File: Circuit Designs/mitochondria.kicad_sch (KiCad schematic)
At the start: 97 parts

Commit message: deleted previous version files
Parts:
- C100, C101, C102, C103, C104, C105, C106, C107, C108, C109, C110, C111, C112, C113, C56, C57, C58, C59, C60, C61, C62, C63, C64, C65, C66, C67, C68, C69, C70, C71, C72, C73, C74, C75, C76, C77, C78, C79, C89, C90, C91, C92, C93, C94, C95, C96, C97, C98, C99: renamed from C?; footprint Capacitor_SMD:C_0402_1005Metric -> CoF_Capacitor:C-0402
- C80, C81, C82, C83, C84, C85, C86, C87, C88: renamed from C?; footprint Capacitor_SMD:C_0805_2012Metric -> CoF_Capacitor:C-0805
- R36, R37, R38, R39, R40, R41, R42, R43, R44, R45, R46, R47, R48, R49, R50, R51, R52, R53, R54, R55, R56, R57, R58, R59, R60, R61, R62, R63, R64, R65, R66, R67: renamed from R?; footprint Resistor_SMD:R_0402_1005Metric -> CoF_Resistor:R-0402
- gave numbers to parts that had none: 7

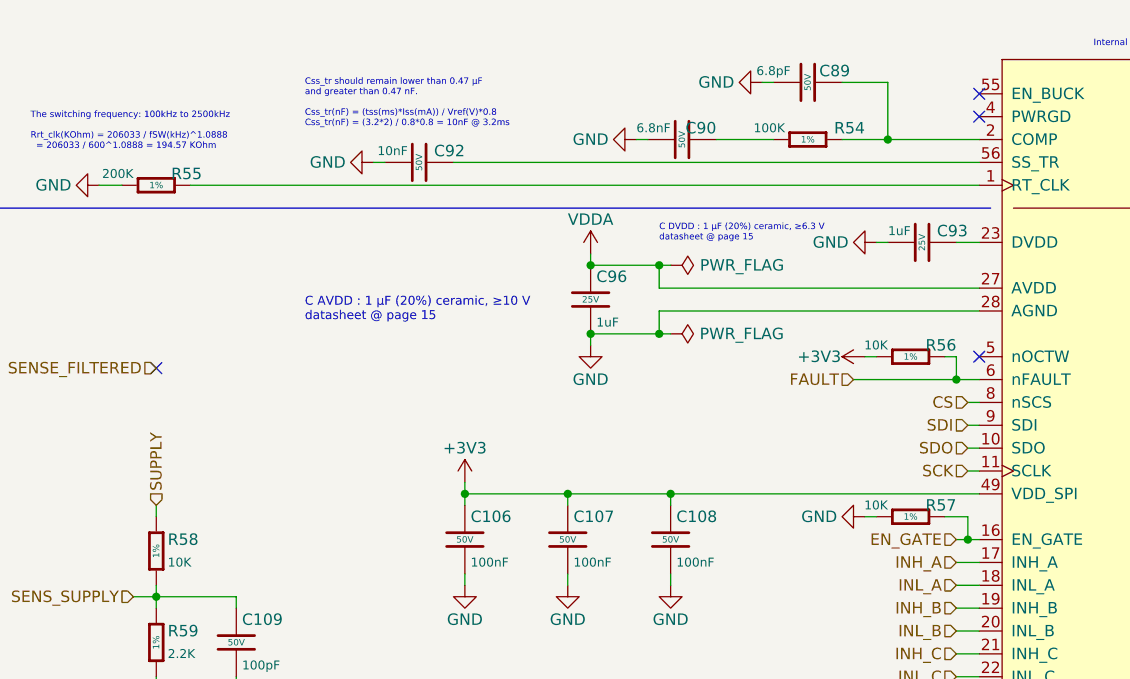
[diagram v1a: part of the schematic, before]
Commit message: changed the LED packages, edited field reference positions
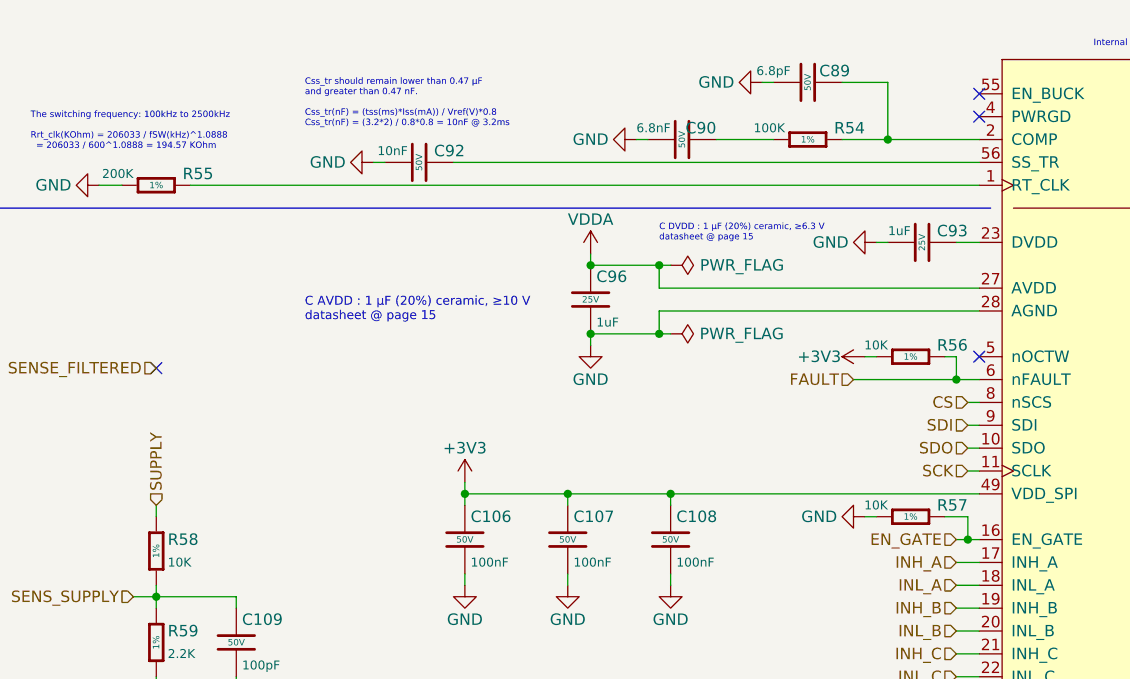
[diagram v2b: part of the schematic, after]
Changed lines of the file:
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@@
   (symbol (lib_id "CoE_Resistor:200K") (at 33.02 99.06 90) (unit 1)
     (in_bom yes) (on_board yes)
-    (property "Reference" "R55" (id 0) (at 38.1 97.79 90)
+    (property "Reference" "R55" (id 0) (at 39.37 97.79 90)
       (effects (font (size 1.27 1.27)) (justify left))
     )
@@
   (symbol (lib_id "CoE_Resistor:10K") (at 116.84 135.89 90) (unit 1)
     (in_bom yes) (on_board yes)
-    (property "Reference" "R57" (id 0) (at 121.92 134.62 90)
+    (property "Reference" "R57" (id 0) (at 123.19 134.62 90)
       (effects (font (size 1.27 1.27)) (justify left))
     )
@@
   (symbol (lib_id "CoE_Resistor:10K") (at 116.84 118.11 90) (unit 1)
     (in_bom yes) (on_board yes)
-    (property "Reference" "R56" (id 0) (at 121.92 116.84 90)
-      (effects (font (size 1.27 1.27)) (justify left))
-    )
+    (property "Reference" "R56" (id 0) (at 123.19 116.84 90)
+      (effects (font (size 1.27 1.27)) (justify left))
+    )

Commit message: added a diode package to the libs
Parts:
- D18: footprint Diode_SMD:D_SOD-123 -> CoF_Diode:SOD-123
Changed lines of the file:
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@@
       (effects (font (size 0.9906 0.9906)) (justify left))
     )
-    (property "Footprint" "Diode_SMD:D_SOD-123" (id 2) (at 224.79 96.52 0)
+    (property "Footprint" "CoF_Diode:SOD-123" (id 2) (at 224.79 96.52 0)
       (effects (font (size 1.27 1.27)) (justify bottom) hide)
     )
-    (property "Datasheet" "https://datasheet.lcsc.com/lcsc/1809140216_Changjiang-Electronics-Tech--CJ-B5819W-SL_C8598.pdf" (id 3) (at 213.106 109.982 0)
+    (property "Datasheet" "https://datasheet.lcsc.com/lcsc/1809140216_Changjiang-Electronics-Tech--CJ-B5819W-SL_C8598.pdf" (id 3) (at 198.12 96.52 0)
       (effects (font (size 1.27 1.27)) hide)
     )

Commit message: created and added the packages called SOT-23-5 and SOT-23-8 to the libraries
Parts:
- U3, U4, U5, U6: footprint Package_TO_SOT_SMD:SOT-23-5 -> CoF_SmallOutline:SOT-23-5
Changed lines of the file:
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@@
       (effects (font (size 0.9906 0.9906)) (justify left))
     )
-    (property "Footprint" "Package_TO_SOT_SMD:SOT-23-5" (id 2) (at 31.115 17.145 0)
-      (effects (font (size 1.27 1.27)) hide)
-    )
-    (property "Datasheet" "https://www.diodes.com/assets/Datasheets/AP2127.pdf" (id 3) (at 31.75 22.86 0)
+    (property "Footprint" "CoF_SmallOutline:SOT-23-5" (id 2) (at 31.115 17.145 0)
+      (effects (font (size 1.27 1.27)) hide)
+    )
+    (property "Datasheet" "https://www.diodes.com/assets/Datasheets/AP2127.pdf" (id 3) (at 31.75 49.53 0)
       (effects (font (size 1.27 1.27)) hide)
     )
@@
       (effects (font (size 0.9906 0.9906)) (justify left))
     )
-    (property "Footprint" "Package_TO_SOT_SMD:SOT-23-5" (id 2) (at 98.425 17.145 0)
-      (effects (font (size 1.27 1.27)) hide)
-    )
-    (property "Datasheet" "https://www.diodes.com/assets/Datasheets/AP2127.pdf" (id 3) (at 99.06 22.86 0)
+    (property "Footprint" "CoF_SmallOutline:SOT-23-5" (id 2) (at 98.425 17.145 0)
+      (effects (font (size 1.27 1.27)) hide)
+    )
+    (property "Datasheet" "https://www.diodes.com/assets/Datasheets/AP2127.pdf" (id 3) (at 99.06 49.53 0)
       (effects (font (size 1.27 1.27)) hide)
     )
@@
       (effects (font (size 0.9906 0.9906)) (justify left))
     )
-    (property "Footprint" "Package_TO_SOT_SMD:SOT-23-5" (id 2) (at 165.735 17.145 0)
-      (effects (font (size 1.27 1.27)) hide)
-    )
-    (property "Datasheet" "https://www.diodes.com/assets/Datasheets/AP2127.pdf" (id 3) (at 166.37 22.86 0)
+    (property "Footprint" "CoF_SmallOutline:SOT-23-5" (id 2) (at 165.735 17.145 0)
+      (effects (font (size 1.27 1.27)) hide)
+    )
+    (property "Datasheet" "https://www.diodes.com/assets/Datasheets/AP2127.pdf" (id 3) (at 166.37 49.53 0)
       (effects (font (size 1.27 1.27)) hide)
     )
@@
       (effects (font (size 0.9906 0.9906)) (justify left))
     )
-    (property "Footprint" "Package_TO_SOT_SMD:SOT-23-5" (id 2) (at 233.045 17.145 0)
-      (effects (font (size 1.27 1.27)) hide)
-    )
-    (property "Datasheet" "https://www.diodes.com/assets/Datasheets/AP2127.pdf" (id 3) (at 233.68 22.86 0)
-      (effects (font (size 1.27 1.27)) hide)
-    )
+    (property "Footprint" "CoF_SmallOutline:SOT-23-5" (id 2) (at 233.045 17.145 0)
+      (effects (font (size 1.27 1.27)) hide)
+    )
+    (property "Datasheet" "https://www.diodes.com/assets/Datasheets/AP2127.pdf" (id 3) (at 233.68 49.53 0)
+      (effects (font (size 1.27 1.27)) hide)
+    )

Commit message: done all the packages and migrations. Now, time to start to route the module
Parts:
- L1: footprint Inductor_SMD:L_Taiyo-Yuden_NR-60xx -> CoF_Inductor:L-7.1-6.6
- U7: footprint Package_SO:HTSSOP-56-1EP_6.1x14mm_P0.5mm_EP3.61x6.35mm -> CoF_SmallOutline:HTSSOP-56-EP

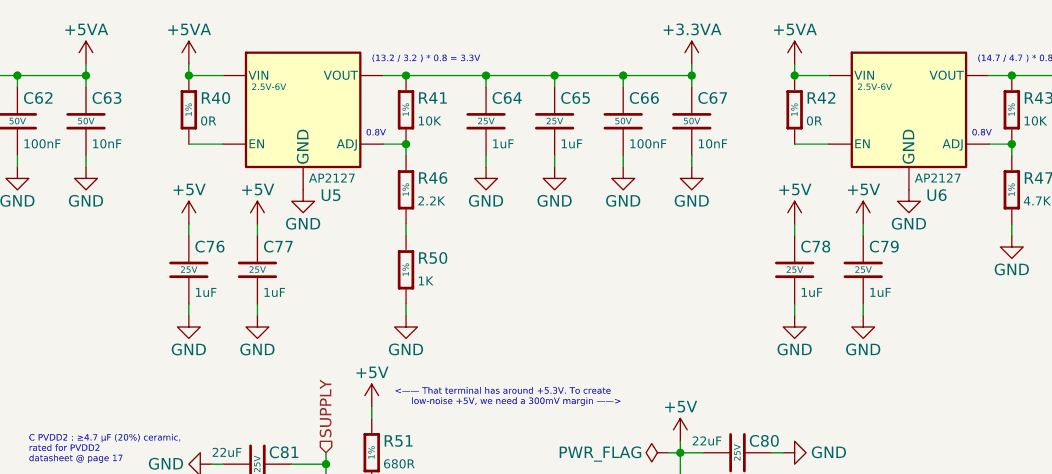
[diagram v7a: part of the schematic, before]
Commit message: First placement of the MCU Page's components are done
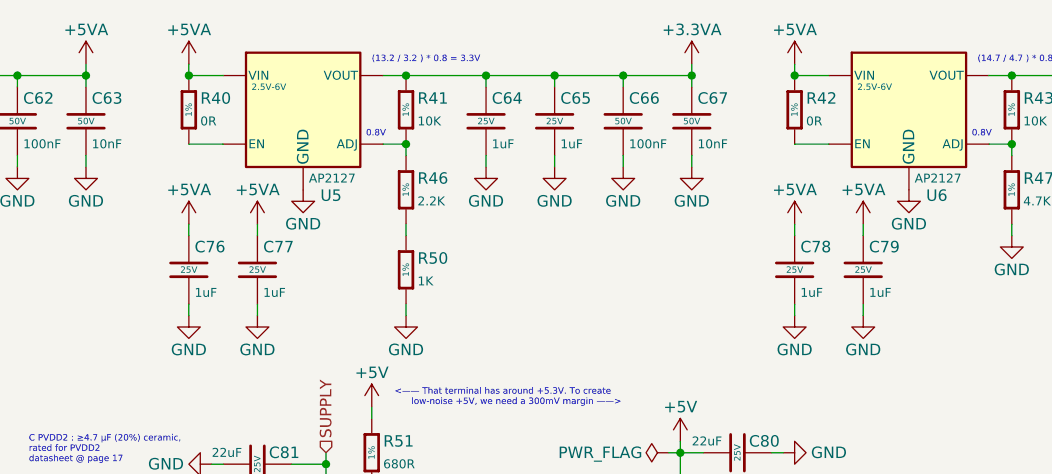
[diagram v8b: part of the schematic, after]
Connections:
- net +5V: no longer C76.1, C77.1, C78.1, C79.1
- net +5VA: now also C76.1, C77.1, C78.1, C79.1
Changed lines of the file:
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@@
-    (pin "1")
-  )
-  (symbol (lib_id "power:+5V") (at 153.67 38.1 0) (unit 1)
-    (in_bom yes) (on_board yes)
-    (property "Reference" "#PWR0112" (id 0) (at 153.67 41.91 0)
-      (effects (font (size 1.27 1.27)) hide)
-    )
-    (property "Value" "+5V" (id 1) (at 153.67 34.29 0))
-    (property "Footprint" "" (id 2) (at 153.67 38.1 0)
-      (effects (font (size 1.27 1.27)) hide)
-    )
-    (property "Datasheet" "" (id 3) (at 153.67 38.1 0)
-      (effects (font (size 1.27 1.27)) hide)
-    )
     (pin "1")
   )
@@
     (pin "2")
   )
-  (symbol (lib_id "power:+5V") (at 161.29 38.1 0) (unit 1)
-    (in_bom yes) (on_board yes)
-    (property "Reference" "#PWR0113" (id 0) (at 161.29 41.91 0)
-      (effects (font (size 1.27 1.27)) hide)
-    )
-    (property "Value" "+5V" (id 1) (at 161.29 34.29 0))
-    (property "Footprint" "" (id 2) (at 161.29 38.1 0)
-      (effects (font (size 1.27 1.27)) hide)
-    )
-    (property "Datasheet" "" (id 3) (at 161.29 38.1 0)
-      (effects (font (size 1.27 1.27)) hide)
-    )
-    (pin "1")
-  )
   (symbol (lib_id "power:GND") (at 93.98 48.26 0) (mirror y) (unit 1)
     (in_bom yes) (on_board yes)
@@
     (pin "1")
   )
-  (symbol (lib_id "power:+5V") (at 220.98 38.1 0) (unit 1)
-    (in_bom yes) (on_board yes)
-    (property "Reference" "#PWR0114" (id 0) (at 220.98 41.91 0)
-      (effects (font (size 1.27 1.27)) hide)
-    )
-    (property "Value" "+5V" (id 1) (at 220.98 34.29 0))
-    (property "Footprint" "" (id 2) (at 220.98 38.1 0)
-      (effects (font (size 1.27 1.27)) hide)
-    )
-    (property "Datasheet" "" (id 3) (at 220.98 38.1 0)
-      (effects (font (size 1.27 1.27)) hide)
-    )
-    (pin "1")
-  )
   (symbol (lib_id "CoE_Capacitor:1uF") (at 228.6 43.18 0) (unit 1)
     (in_bom yes) (on_board yes)
@@
     (pin "1")
     (pin "2")
-  )
-  (symbol (lib_id "power:+5V") (at 228.6 38.1 0) (unit 1)
-    (in_bom yes) (on_board yes)
-    (property "Reference" "#PWR0115" (id 0) (at 228.6 41.91 0)
-      (effects (font (size 1.27 1.27)) hide)
-    )
-    (property "Value" "+5V" (id 1) (at 228.6 34.29 0))
-    (property "Footprint" "" (id 2) (at 228.6 38.1 0)
-      (effects (font (size 1.27 1.27)) hide)
-    )
-    (property "Datasheet" "" (id 3) (at 228.6 38.1 0)
-      (effects (font (size 1.27 1.27)) hide)
-    )
-    (pin "1")
   )
   (symbol (lib_id "power:PWR_FLAG") (at 90.17 115.57 270) (unit 1)
@@
       (effects (font (size 1.27 1.27)) hide)
     )
+    (pin "1")
+  )
+  (symbol (lib_id "power:+5VA") (at 161.29 38.1 0) (unit 1)
+    (in_bom yes) (on_board yes)
+    (property "Reference" "#PWR?" (id 0) (at 161.29 41.91 0)
+      (effects (font (size 1.27 1.27)) hide)
+    )
+    (property "Value" "+5VA" (id 1) (at 161.29 34.29 0))
+    (property "Footprint" "" (id 2) (at 161.29 38.1 0)
+      (effects (font (size 1.27 1.27)) hide)
+    )
+    (property "Datasheet" "" (id 3) (at 161.29 38.1 0)
+      (effects (font (size 1.27 1.27)) hide)
+    )
+    (pin "1")
+  )
+  (symbol (lib_id "power:+5VA") (at 153.67 38.1 0) (unit 1)
+    (in_bom yes) (on_board yes)
+    (property "Reference" "#PWR?" (id 0) (at 153.67 41.91 0)
+      (effects (font (size 1.27 1.27)) hide)
+    )
+    (property "Value" "+5VA" (id 1) (at 153.67 34.29 0))
+    (property "Footprint" "" (id 2) (at 153.67 38.1 0)
+      (effects (font (size 1.27 1.27)) hide)
+    )
+    (property "Datasheet" "" (id 3) (at 153.67 38.1 0)
+      (effects (font (size 1.27 1.27)) hide)
+    )
+    (pin "1")
+  )
+  (symbol (lib_id "power:+5VA") (at 228.6 38.1 0) (unit 1)
+    (in_bom yes) (on_board yes)
+    (property "Reference" "#PWR?" (id 0) (at 228.6 41.91 0)
+      (effects (font (size 1.27 1.27)) hide)
+    )
+    (property "Value" "+5VA" (id 1) (at 228.6 34.29 0))
+    (property "Footprint" "" (id 2) (at 228.6 38.1 0)
+      (effects (font (size 1.27 1.27)) hide)
+    )
+    (property "Datasheet" "" (id 3) (at 228.6 38.1 0)
+      (effects (font (size 1.27 1.27)) hide)
+    )
+    (pin "1")
+  )
+  (symbol (lib_id "power:+5VA") (at 220.98 38.1 0) (unit 1)
+    (in_bom yes) (on_board yes)
+    (property "Reference" "#PWR?" (id 0) (at 220.98 41.91 0)
+      (effects (font (size 1.27 1.27)) hide)
+    )
+    (property "Value" "+5VA" (id 1) (at 220.98 34.29 0))
+    (property "Footprint" "" (id 2) (at 220.98 38.1 0)
+      (effects (font (size 1.27 1.27)) hide)
+    )
+    (property "Datasheet" "" (id 3) (at 220.98 38.1 0)
+      (effects (font (size 1.27 1.27)) hide)
+    )
